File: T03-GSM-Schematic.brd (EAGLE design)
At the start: 33.8 x 80.3 mm, 20 parts, among them J1 5.5x2.1mm Barrel, J2 AVR_SPI_PRG_62X3_LOCK, Q2 16M, U1 ATMEGA328P-PU, U2 LM317MDT-TR

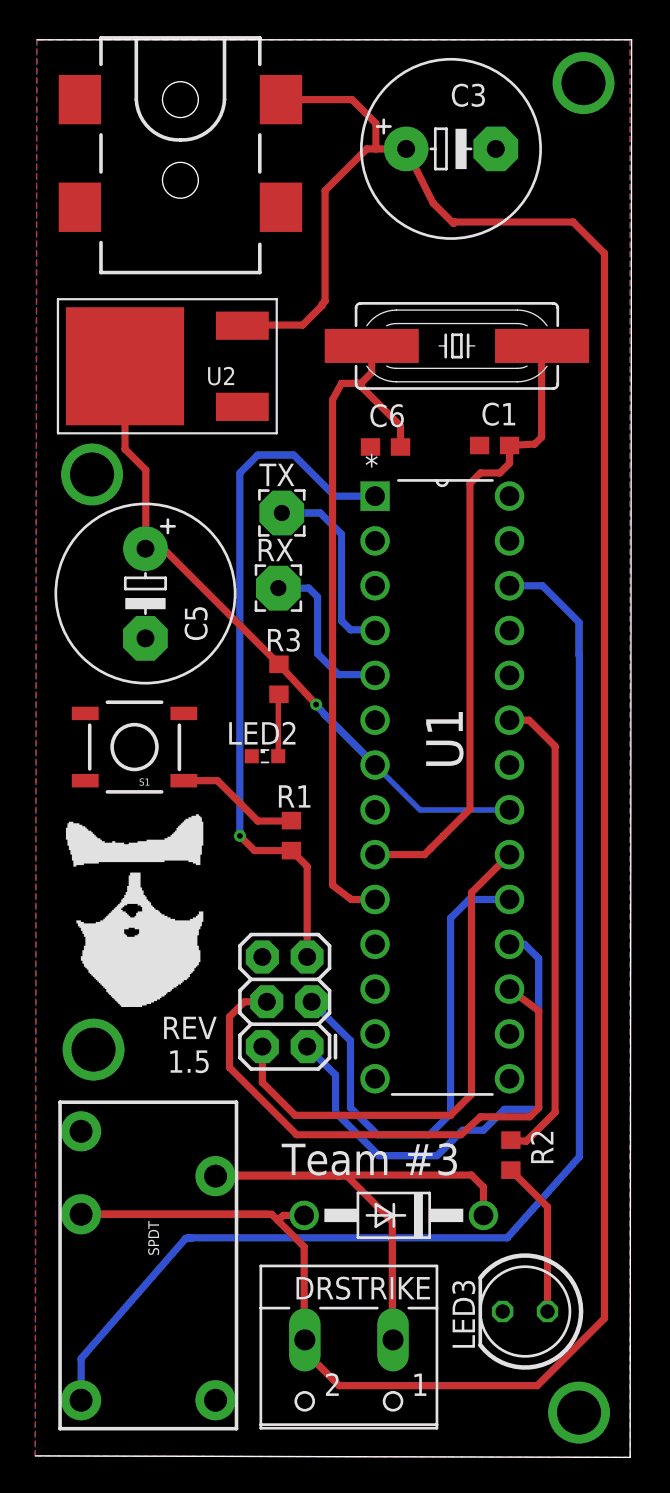
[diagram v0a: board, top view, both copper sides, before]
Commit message: changed the Power Jack to through hole
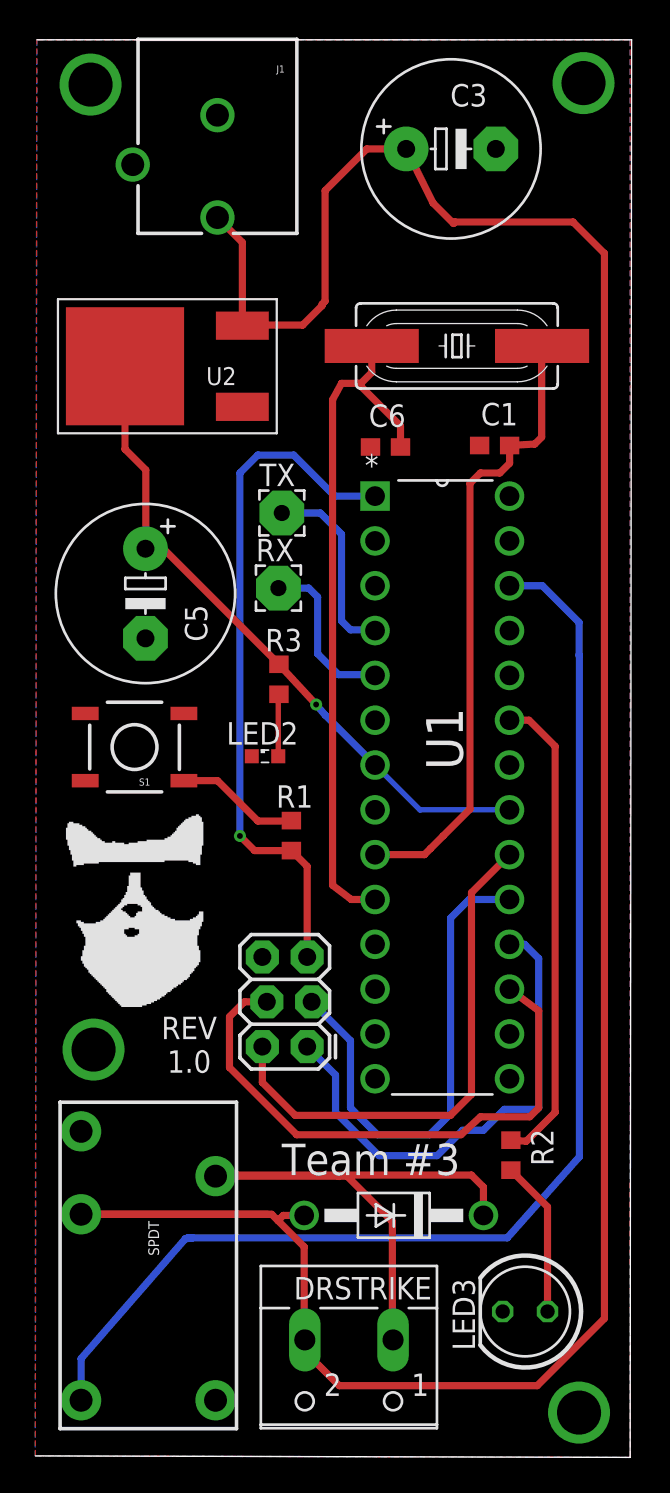
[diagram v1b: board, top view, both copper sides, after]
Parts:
- J1: value 5.5x2.1mm Barrel -> POWER_JACKPTH_BREAD; device SparkFun-Connectors:POWER_JACK_SMD -> SparkFun-Connectors:POWER_JACK_PTH_BREAD
- moved J1 7.33 mm to (10.2, 83.6), turned to 180 degrees
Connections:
- net 12V: now also J1.PWR; no longer J1.VIN0
- net GND: now also J1.GND; no longer J1.P$4
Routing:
- net 12V: track 150.9 -> 150.3 mm
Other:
- board text added: "REV 1.0"
- board text removed: "REV 1.5"
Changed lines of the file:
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@@
 <rectangle x1="9.01811875" y1="36.02349375" x2="9.18575625" y2="36.108075" layer="21"/>
 <text x="8.6351375" y="24.635534375" size="1.27" layer="21" font="vector" rot="R180" align="bottom-center">REV
-1.5</text>
+1.0</text>
 <text x="13.883946875" y="15.661765625" size="1.778" layer="21">Team #3</text>
 <dimension x1="33.627971875" y1="79.999996875" x2="33.627971875" y2="-0.33863125" x3="39.6200375" y3="39.83068125" textsize="1.778" layer="20" visible="yes"/>
 <dimension x1="0" y1="80" x2="33.627971875" y2="79.999996875" x3="16.8139875" y3="88.21385" textsize="1.778" layer="20" visible="yes"/>
-<dimension x1="0" y1="80" x2="3.55564375" y2="80.002" x3="1.775346875" y3="84.40284375" textsize="1.778" layer="20" visible="yes"/>
 </plain>
 <attributes>
@@
 </class>
 </classes>
-<designrules name="OSH-Park-2-layer">
+<designrules name="OSH-Park-2-layer *">
 <description language="de">&lt;b&gt;EAGLE Design Rules&lt;/b&gt;
 &lt;p&gt;
@@
 <param name="mdPadVia" value="6mil"/>
 <param name="mdViaVia" value="6mil"/>
-<param name="mdSmdPad" value="6mil"/>
-<param name="mdSmdVia" value="6mil"/>
-<param name="mdSmdSmd" value="6mil"/>
+<param name="mdSmdPad" value="0mil"/>
+<param name="mdSmdVia" value="0mil"/>
+<param name="mdSmdSmd" value="0mil"/>
 <param name="mdViaViaSameLayer" value="8mil"/>
 <param name="mnLayersViaInSmd" value="2"/>
@@
 <attribute name="NAME" x="22.38278125" y="9.884484375" size="1.27" layer="25" ratio="10" rot="R180"/>
 </element>
-<element name="J1" library="SparkFun-Connectors" package="POWER_JACK_SMD" value="5.5x2.1mm Barrel" x="8.14" y="76.61" rot="R270">
-<attribute name="SF_ID" value="PRT-12748" x="8.14" y="76.61" size="1.778" layer="27" rot="R270" display="off"/>
-<attribute name="PROD_ID" value="CONN-08106" x="8.14" y="76.61" size="1.778" layer="27" rot="R270" display="off"/>
+<element name="J1" library="SparkFun-Connectors" package="POWER_JACK_PTH_BREAD" value="POWER_JACKPTH_BREAD" x="10.237971875" y="83.629490625" rot="R180">
+<attribute name="PROD_ID" value="PRT-10811" x="10.237971875" y="83.629490625" size="1.778" layer="27" rot="R180" display="off"/>
 </element>
 <element name="LED2" library="led" package="SML0603" value="" x="12.935275" y="39.39726875" smashed="yes">
@@
 <contactref element="U1" pad="22"/>
 <contactref element="S1" pad="3"/>
-<contactref element="J1" pad="P$4"/>
+<contactref element="J1" pad="GND"/>
 <contactref element="C5" pad="-"/>
 <contactref element="SPDT" pad="1"/>
@@
 <wire x1="6.15931875" y1="51.158884375" x2="7.175215625" y2="51.158884375" width="0.4064" layer="1"/>
 <wire x1="7.175215625" y1="51.158884375" x2="13.72341875" y2="44.61068125" width="0.4064" layer="1"/>
-<wire x1="26.79" y1="33.82" x2="26.79" y2="36.36" width="0" layer="19" extent="1-1"/>
 <wire x1="5" y1="61.5" x2="5" y2="56.8004875" width="0.4064" layer="1"/>
 <wire x1="6.18005" y1="55.6204375" x2="6.18005" y2="51.179615625" width="0.4064" layer="1"/>
+<wire x1="26.79" y1="33.82" x2="26.79" y2="36.36" width="0" layer="19" extent="1-1"/>
 </signal>
 <signal name="N$1">
@@
 <contactref element="D1" pad="A"/>
 <wire x1="2.51" y1="13.441" x2="13.1215125" y2="13.441" width="0.4064" layer="1"/>
-<wire x1="20.933709375" y1="73.816803125" x2="19.2174125" y2="73.816803125" width="0.4064" layer="1"/>
-<wire x1="19.2174125" y1="73.816803125" x2="18.7043125" y2="73.816803125" width="0.4064" layer="1"/>
+<wire x1="20.933709375" y1="73.816803125" x2="18.7043125" y2="73.816803125" width="0.4064" layer="1"/>
 <wire x1="18.7043125" y1="73.816803125" x2="16.33903125" y2="71.451521875" width="0.4064" layer="1"/>
 <wire x1="16.33903125" y1="71.451521875" x2="16.33903125" y2="65.1868125" width="0.4064" layer="1"/>
@@
 <wire x1="12.44475625" y1="63.916940625" x2="11.766940625" y2="63.916940625" width="0.4064" layer="1"/>
 <wire x1="11.766940625" y1="63.916940625" x2="11.65" y2="63.8" width="0.4064" layer="1"/>
-<contactref element="J1" pad="VIN0"/>
-<wire x1="13.84" y1="76.61" x2="17.868553125" y2="76.61" width="0.4064" layer="1"/>
-<wire x1="17.868553125" y1="76.61" x2="19.2174125" y2="75.261140625" width="0.4064" layer="1"/>
-<wire x1="19.2174125" y1="75.261140625" x2="19.2174125" y2="73.816803125" width="0.4064" layer="1"/>
+<contactref element="J1" pad="PWR"/>
 <wire x1="15.153309375" y1="13.375996875" x2="13.96860625" y2="13.375996875" width="0.4064" layer="1"/>
 <wire x1="13.96860625" y1="13.375996875" x2="13.6723" y2="13.079690625" width="0.4064" layer="1"/>
@@
 <wire x1="23.704296875" y1="69.6737" x2="30.39229375" y2="69.6737" width="0.4064" layer="1"/>
 <wire x1="30.39229375" y1="69.6737" x2="32.170115625" y2="67.895878125" width="0.4064" layer="1"/>
-<wire x1="17.0886625" y1="3.7734375" x2="16.780415625" y2="4.081684375" width="0.4064" layer="1"/>
-<wire x1="16.780415625" y1="4.081684375" x2="15.19" y2="5.6721" width="0.4064" layer="1"/>
+<wire x1="17.137140625" y1="3.724959375" x2="15.19" y2="5.6721" width="0.4064" layer="1"/>
 <wire x1="32.170115625" y1="67.895878125" x2="32.170115625" y2="7.534578125" width="0.4064" layer="1"/>
 <wire x1="32.170115625" y1="7.534578125" x2="28.360496875" y2="3.724959375" width="0.4064" layer="1"/>
 <wire x1="28.360496875" y1="3.724959375" x2="17.137140625" y2="3.724959375" width="0.4064" layer="1"/>
-<wire x1="17.137140625" y1="3.724959375" x2="17.0886625" y2="3.7734375" width="0.4064" layer="1"/>
+<wire x1="10.237971875" y1="69.929490625" x2="11.65" y2="68.5174625" width="0.4064" layer="1"/>
+<wire x1="11.65" y1="68.5174625" x2="11.65" y2="63.8" width="0.4064" layer="1"/>
 </signal>
 <signal name="N$16">
@@
 <via x="30.730925" y="2.20111875" extent="1-16" drill="2.5"/>
 <via x="3.217009375" y="22.773059375" extent="1-16" drill="2.5"/>
-<via x="3.132353125" y="55.366465625" extent="1-16" drill="2.5"/>
-<wire x1="3.132353125" y1="55.366465625" x2="30.9849" y2="77.546915625" width="0" layer="19" extent="1-1"/>
-<wire x1="3.217009375" y1="22.773059375" x2="3.132353125" y2="55.366465625" width="0" layer="19" extent="1-1"/>
+<via x="3.047696875" y="77.46225625" extent="1-16" drill="2.5"/>
+<wire x1="3.047696875" y1="77.46225625" x2="30.9849" y2="77.546915625" width="0" layer="19" extent="1-1"/>
+<wire x1="3.217009375" y1="22.773059375" x2="3.047696875" y2="77.46225625" width="0" layer="19" extent="1-1"/>
 <wire x1="30.730925" y1="2.20111875" x2="3.217009375" y2="22.773059375" width="0" layer="19" extent="1-1"/>
 </signal>

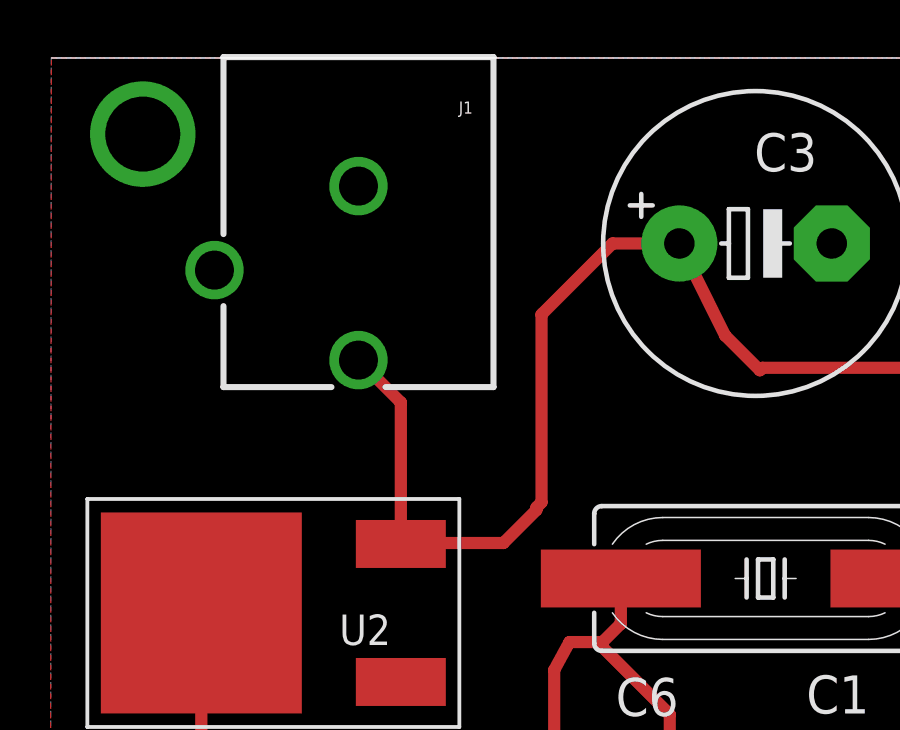
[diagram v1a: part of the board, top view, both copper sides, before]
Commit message: Switched power + and - on power jack
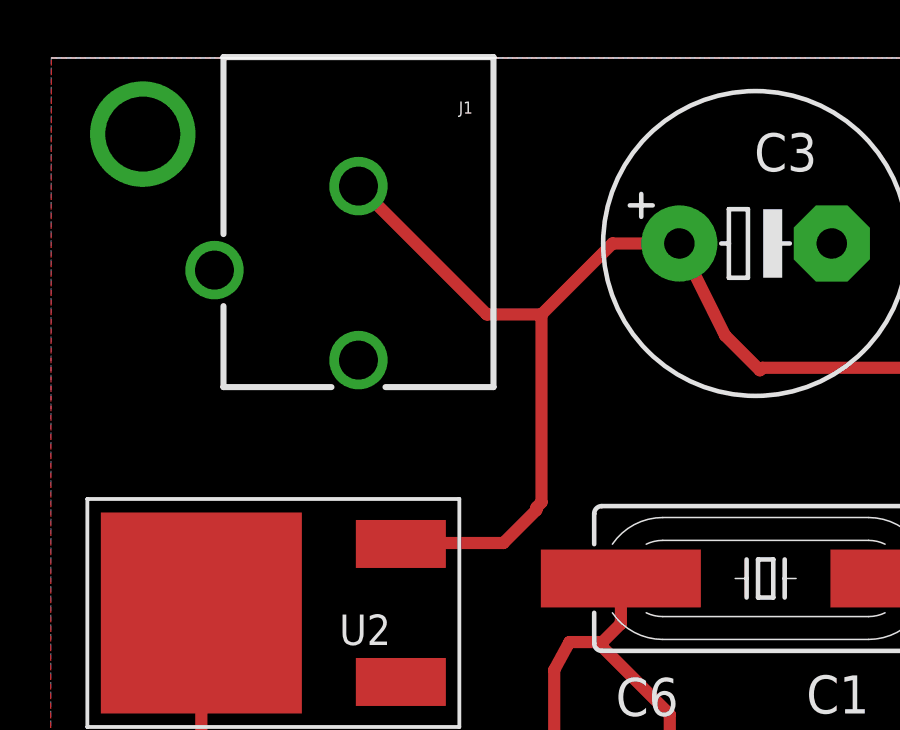
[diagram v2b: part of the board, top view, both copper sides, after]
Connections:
- net 12V: now also J1.GND; no longer J1.PWR
- net GND: now also J1.PWR; no longer J1.GND
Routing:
- net 12V: track 150.3 -> 151.4 mm
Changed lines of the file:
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@@
 </class>
 </classes>
-<designrules name="OSH-Park-2-layer *">
+<designrules name="OSH-Park-2-layer">
 <description language="de">&lt;b&gt;EAGLE Design Rules&lt;/b&gt;
 &lt;p&gt;
@@
 <param name="mdPadVia" value="6mil"/>
 <param name="mdViaVia" value="6mil"/>
-<param name="mdSmdPad" value="0mil"/>
-<param name="mdSmdVia" value="0mil"/>
-<param name="mdSmdSmd" value="0mil"/>
+<param name="mdSmdPad" value="6mil"/>
+<param name="mdSmdVia" value="6mil"/>
+<param name="mdSmdSmd" value="6mil"/>
 <param name="mdViaViaSameLayer" value="8mil"/>
 <param name="mnLayersViaInSmd" value="2"/>
@@
 <contactref element="U1" pad="22"/>
 <contactref element="S1" pad="3"/>
-<contactref element="J1" pad="GND"/>
 <contactref element="C5" pad="-"/>
 <contactref element="SPDT" pad="1"/>
@@
 <contactref element="U2" pad="1"/>
 <contactref element="J2" pad="6"/>
+<contactref element="J1" pad="PWR"/>
+<wire x1="10.237971875" y1="69.929490625" x2="26.013709375" y2="73.816803125" width="0" layer="19" extent="1-1"/>
+<wire x1="11.65" y1="59.2" x2="10.237971875" y2="69.929490625" width="0" layer="19" extent="1-1"/>
+<wire x1="18.913290625" y1="56.92205" x2="11.65" y2="59.2" width="0" layer="19" extent="1-1"/>
+<wire x1="25.097821875" y1="57.0067125" x2="18.913290625" y2="56.92205" width="0" layer="19" extent="1-1"/>
+<wire x1="6.15931875" y1="46.078884375" x2="11.65" y2="59.2" width="0" layer="19" extent="1-1"/>
+<wire x1="8.334003125" y1="41.823075" x2="6.15931875" y2="46.078884375" width="0" layer="19" extent="1-1"/>
+<wire x1="12.185275" y1="39.39726875" x2="8.334003125" y2="41.823075" width="0" layer="19" extent="1-1"/>
+<wire x1="19.17" y1="36.36" x2="12.185275" y2="39.39726875" width="0" layer="19" extent="1-1"/>
+<wire x1="26.79" y1="38.9" x2="19.17" y2="36.36" width="0" layer="19" extent="1-1"/>
+<wire x1="12.783140625" y1="28.022375" x2="19.17" y2="36.36" width="0" layer="19" extent="1-1"/>
+<wire x1="2.51" y1="18.14" x2="12.783140625" y2="28.022375" width="0" layer="19" extent="1-1"/>
+<wire x1="10.13" y1="2.9" x2="2.51" y2="18.14" width="0" layer="19" extent="1-1"/>
+<wire x1="26.40465625" y1="7.928378125" x2="10.13" y2="2.9" width="0" layer="19" extent="1-1"/>
 </signal>
 <signal name="N$3">
@@
 <wire x1="12.44475625" y1="63.916940625" x2="11.766940625" y2="63.916940625" width="0.4064" layer="1"/>
 <wire x1="11.766940625" y1="63.916940625" x2="11.65" y2="63.8" width="0.4064" layer="1"/>
-<contactref element="J1" pad="PWR"/>
 <wire x1="15.153309375" y1="13.375996875" x2="13.96860625" y2="13.375996875" width="0.4064" layer="1"/>
 <wire x1="13.96860625" y1="13.375996875" x2="13.6723" y2="13.079690625" width="0.4064" layer="1"/>
@@
 <wire x1="32.170115625" y1="7.534578125" x2="28.360496875" y2="3.724959375" width="0.4064" layer="1"/>
 <wire x1="28.360496875" y1="3.724959375" x2="17.137140625" y2="3.724959375" width="0.4064" layer="1"/>
-<wire x1="10.237971875" y1="69.929490625" x2="11.65" y2="68.5174625" width="0.4064" layer="1"/>
-<wire x1="11.65" y1="68.5174625" x2="11.65" y2="63.8" width="0.4064" layer="1"/>
+<contactref element="J1" pad="GND"/>
+<wire x1="10.237971875" y1="75.729490625" x2="14.515940625" y2="71.451521875" width="0.4064" layer="1"/>
+<wire x1="14.515940625" y1="71.451521875" x2="16.33903125" y2="71.451521875" width="0.4064" layer="1"/>
 </signal>
 <signal name="N$16">

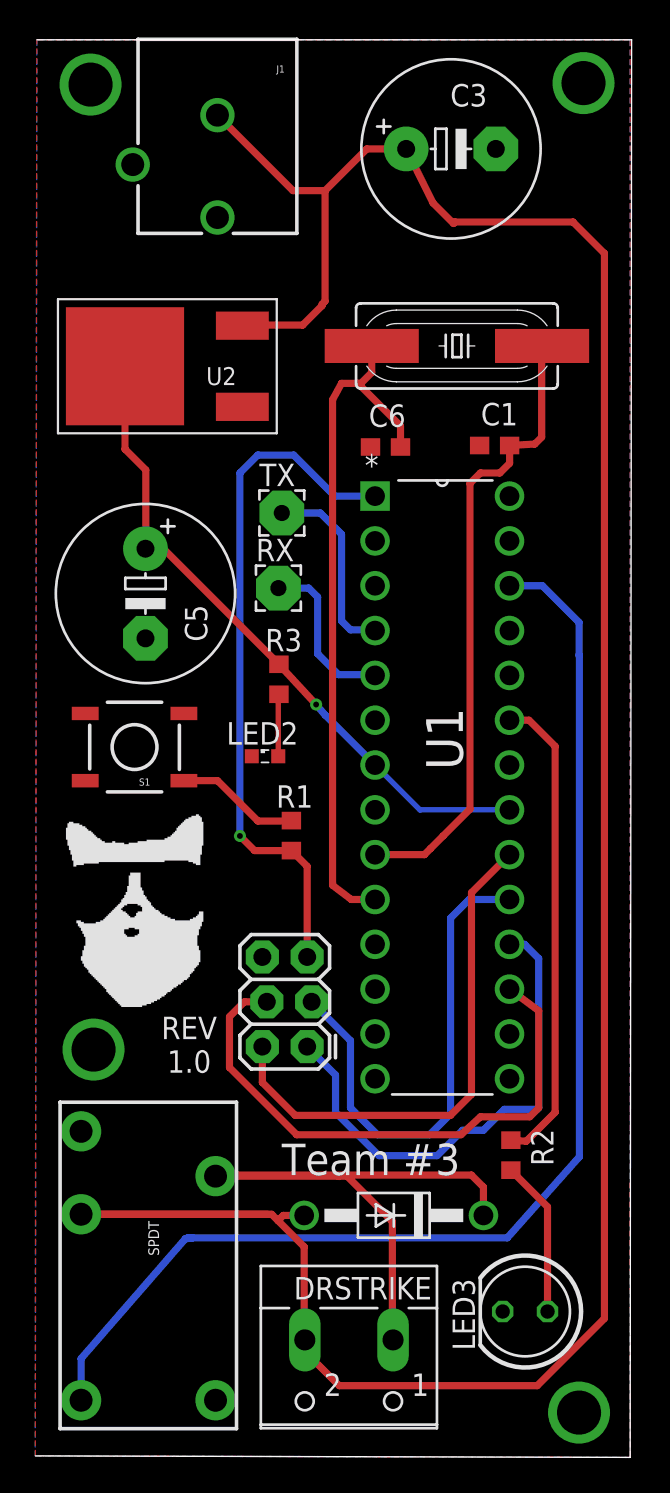
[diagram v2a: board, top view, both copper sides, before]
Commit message: Change the Voltage regulator to through hole
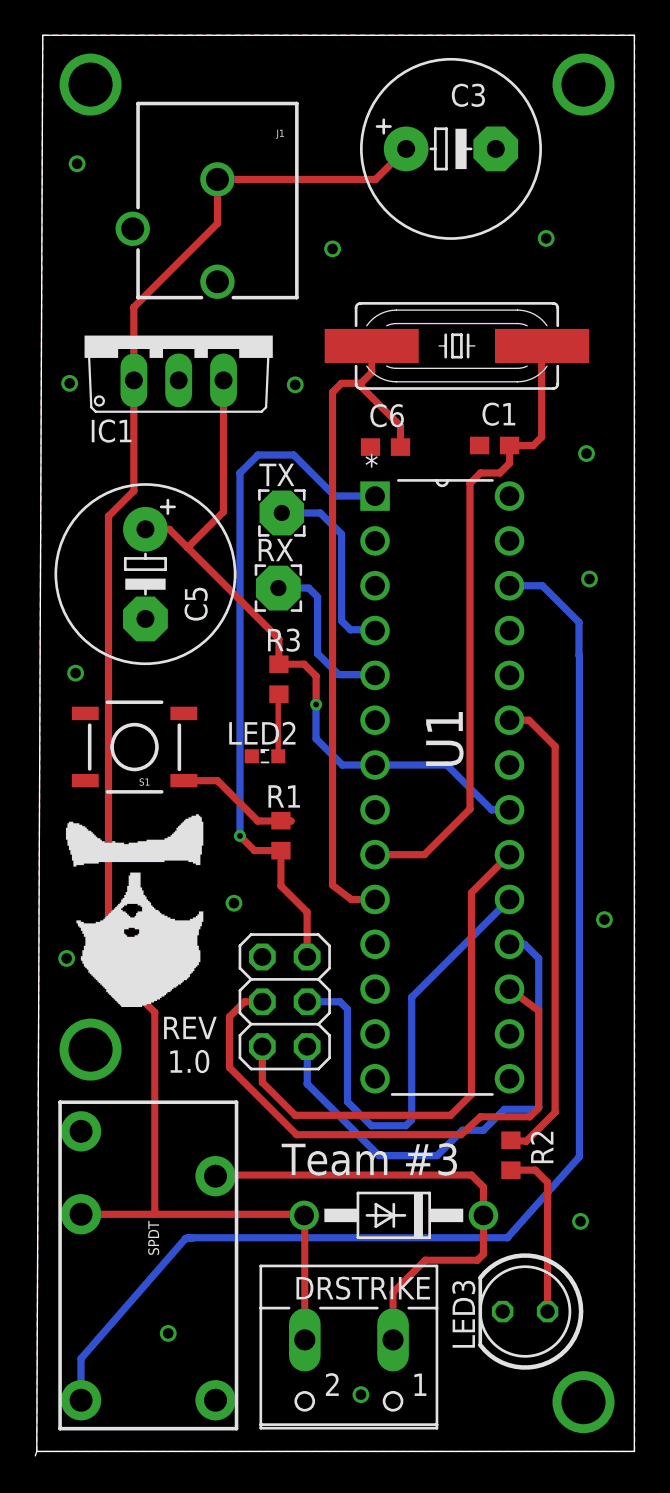
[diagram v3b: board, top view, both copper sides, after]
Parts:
- removed U2: LM317MDT-TR, MF_IC_Power:TO-252-3
- added IC1: 788TV, linear:TO220V
- J2: value AVR_SPI_PRG_62X3_LOCK -> AVR; device SparkFun-Connectors:2X3_LOCK -> pinhead:2X03
- moved J1 3.64 mm to (10.2, 80.0)
- moved J2 2.84 mm to (14.1, 25.5)
- moved C5 1.10 mm to (6.16, 49.7)
- moved R1 0.59 mm to (13.8, 34.9)
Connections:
- net 12V: now also IC1.1; no longer U2.2
- net 5V: now also IC1.3; no longer U2.PAD
- net GND: now also IC1.2; no longer U2.1
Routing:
- net 12V: track 151.4 -> 93.5 mm
- net N$4: track 34.9 -> 28.0 mm
- net 5V: track 67.3 -> 70.1 mm
- net N$5: track 28.6 -> 26.8 mm
- net N$6: track 8.87 -> 9.69 mm
- net N$2: track 7.05 -> 7.59 mm
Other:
- board size 33.8 x 80.3 mm -> 33.9 x 80.5 mm
